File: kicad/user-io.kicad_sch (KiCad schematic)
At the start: 46 parts, among them J1 USB1, J2 Conn_01x30, J3 Conn_01x30, SW1 PTS815, U1 MIMXRT1171DVMAB, U2 MAYA-W166-00B, U3 LSM6DSV, U4 LIS2MDL, U5 RTMC-G2-4IQ48, Y1 8MHz

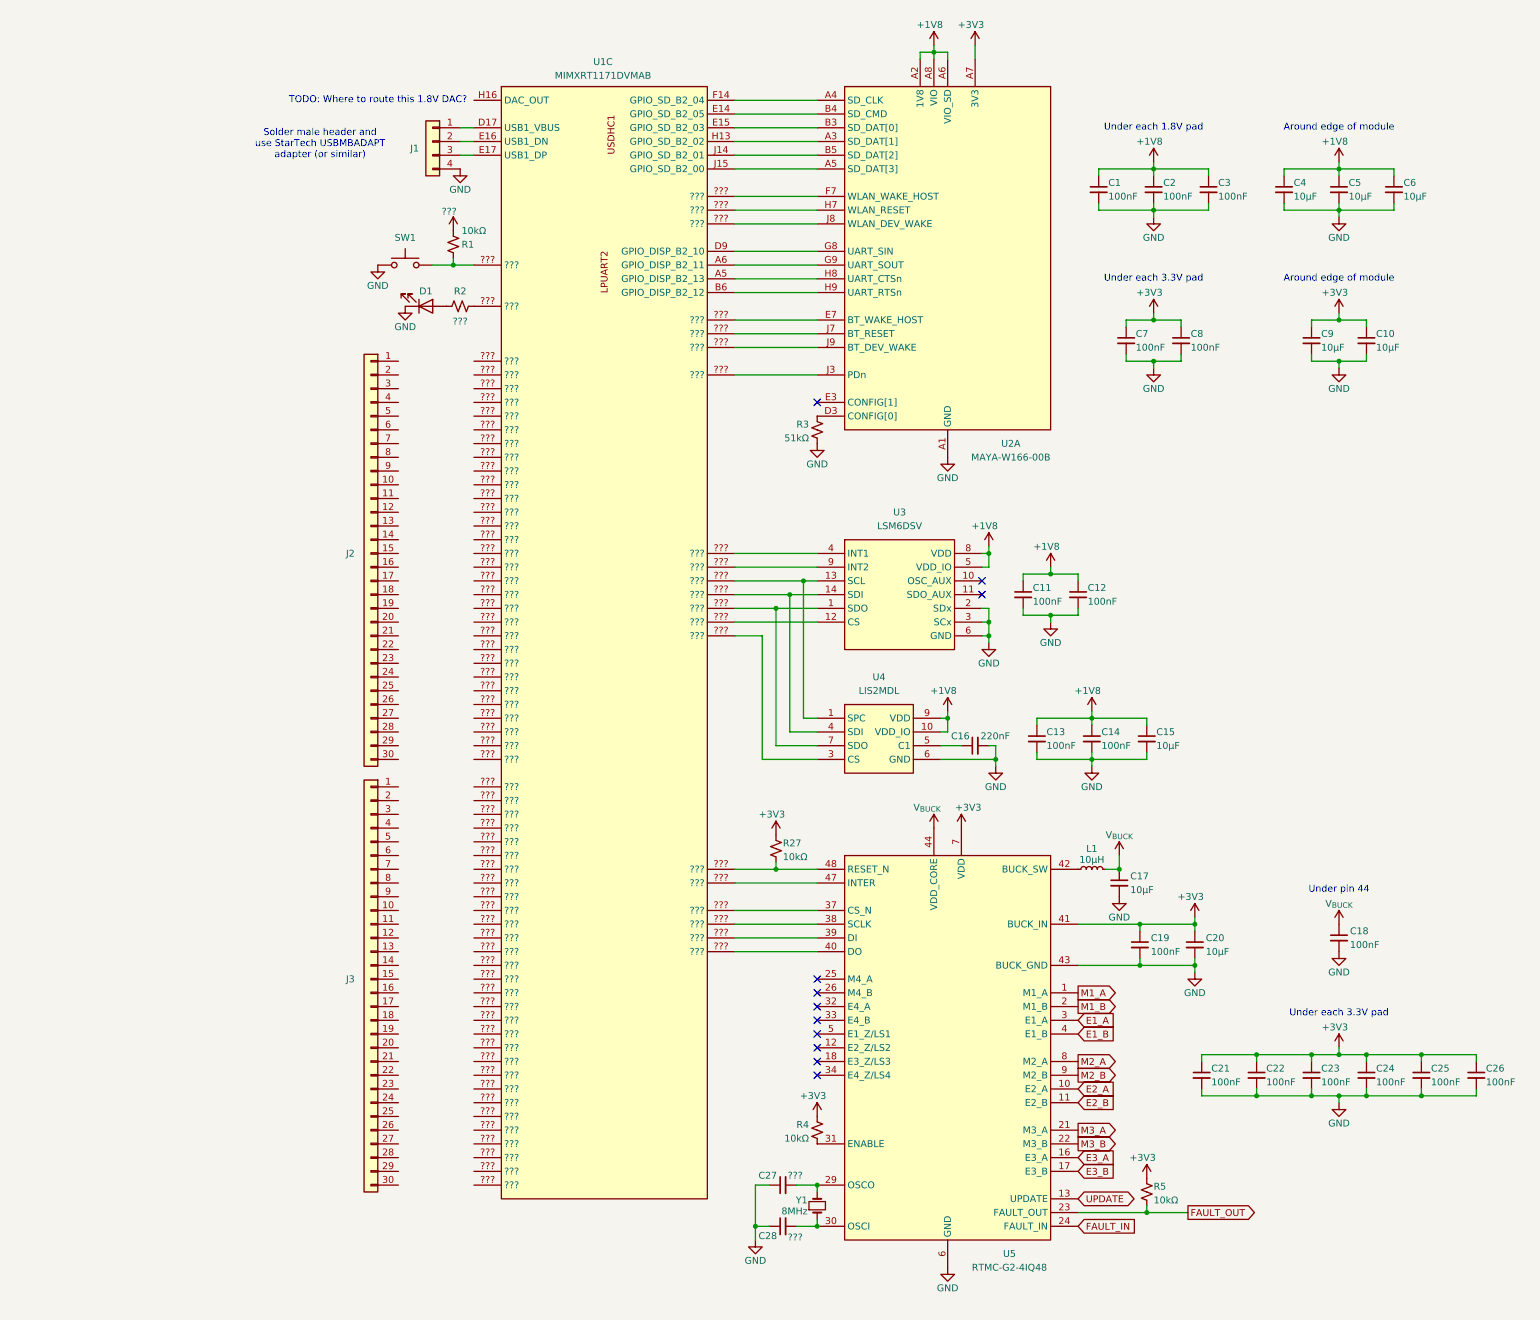
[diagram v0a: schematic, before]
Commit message: added several footprints
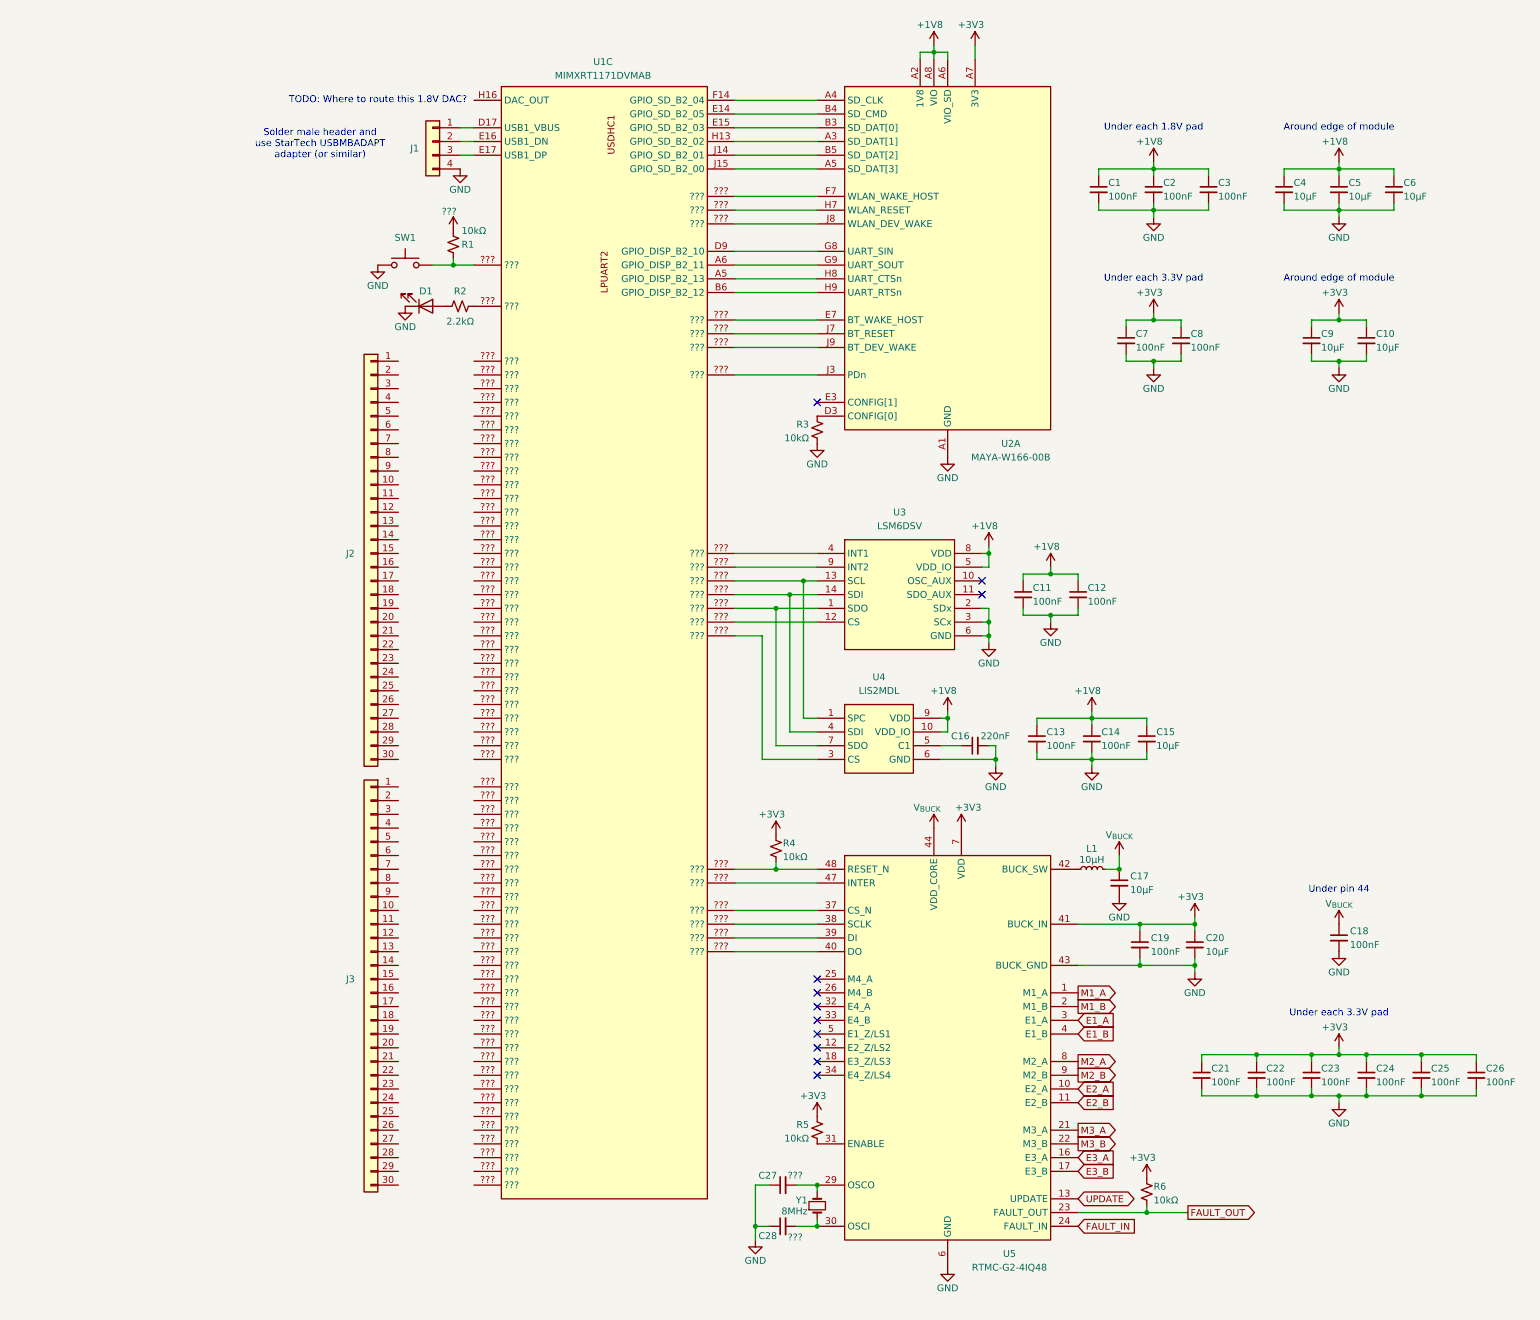
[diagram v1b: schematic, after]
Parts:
- C1, C11, C12, C13, C14, C18, C19, C2, C21, C22, C23, C24, C25, C26, C3, C7, C8: footprint (none) -> Capacitor_SMD:C_0201_0603Metric
- C10, C15, C17, C20, C4, C5, C6, C9: footprint (none) -> Capacitor_SMD:C_0402_1005Metric
- D1: footprint (none) -> LED_SMD:LED_0603_1608Metric
- J1: footprint (none) -> project_footprints:Header-1x04
- J2, J3: value Conn_01x30 -> (none); footprint (none) -> project_footprints:Header-1x30
- R1: footprint (none) -> Resistor_SMD:R_0201_0603Metric
- R2: value ??? -> 2.2kΩ; footprint (none) -> Resistor_SMD:R_0201_0603Metric
- R3: value 51kΩ -> 10kΩ; footprint (none) -> Resistor_SMD:R_0201_0603Metric
- R4: renamed from R27; footprint (none) -> Resistor_SMD:R_0201_0603Metric
- R5: renamed from R4; footprint (none) -> Resistor_SMD:R_0201_0603Metric
- R6: renamed from R5; footprint (none) -> Resistor_SMD:R_0201_0603Metric
- U1: footprint Package_BGA:MAPBGA-289_14x14mm_Layout17x17_P0.8mm -> project_footprints:MIMXRT1171DVMAB
- U3: footprint (none) -> project_footprints:LSM6DSV
- U4: footprint (none) -> project_footprints:LIS2MDL
- U5: footprint (none) -> project_footprints:RTMC-G2-4IQ48
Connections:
- net at U1.???: now also U2.J9 (BT_DEV_WAKE)

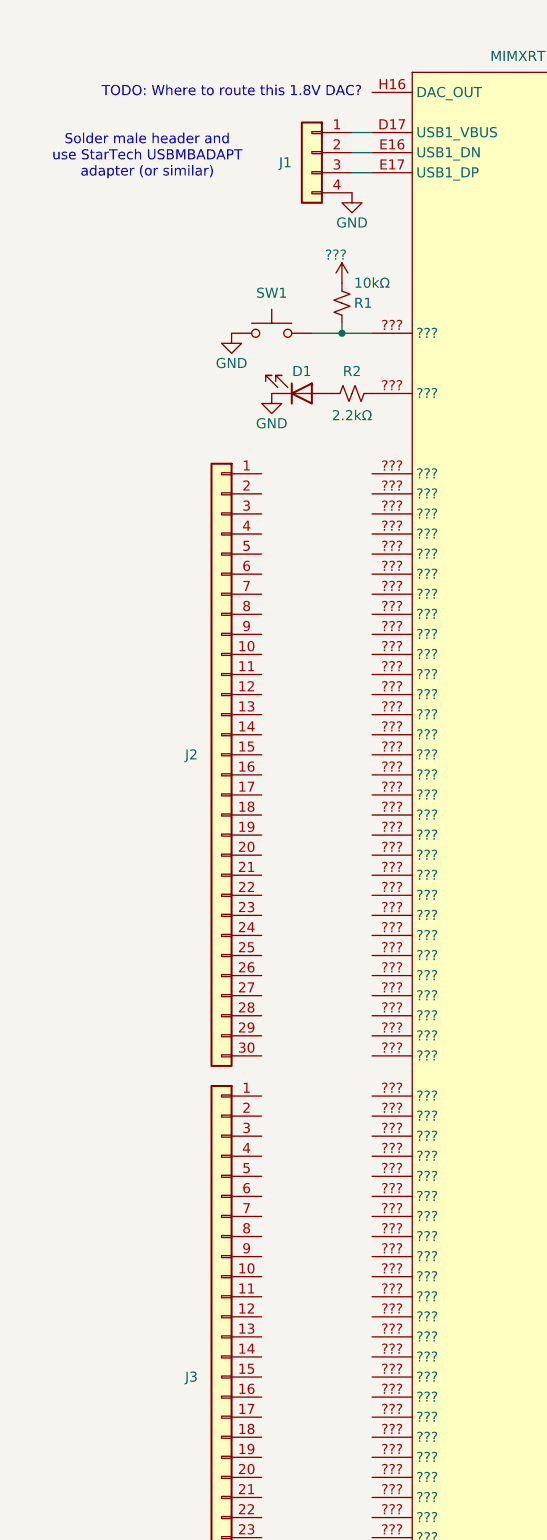
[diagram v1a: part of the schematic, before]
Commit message: added RTC battery connector
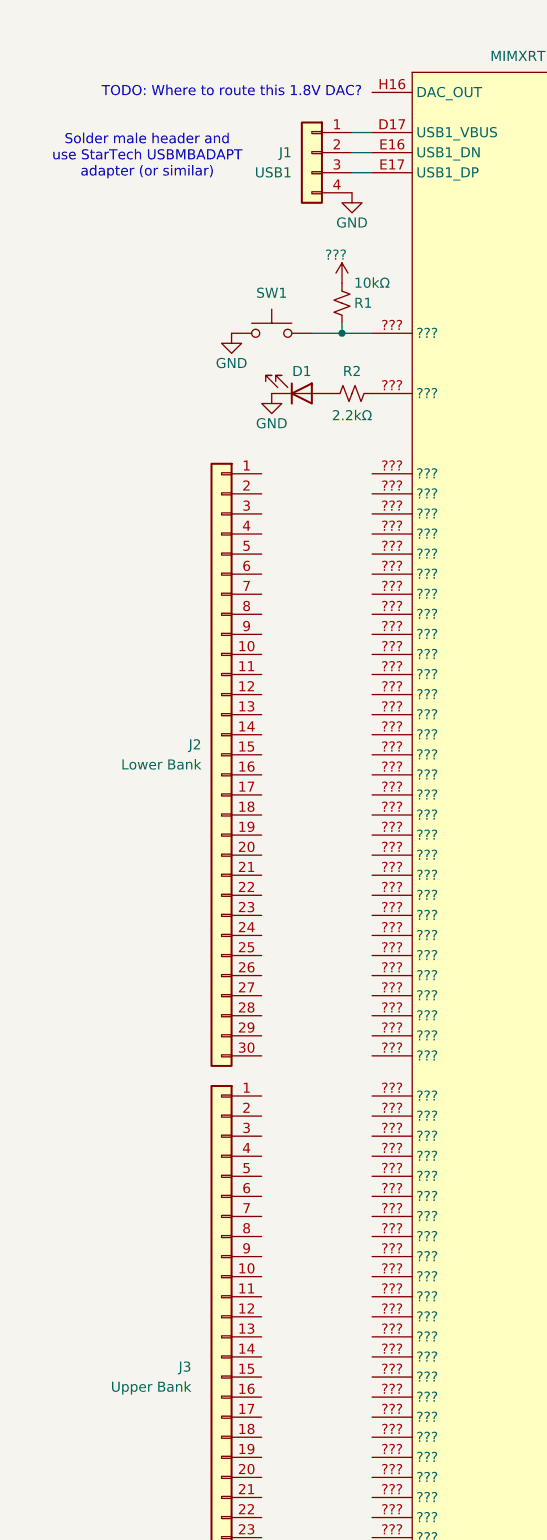
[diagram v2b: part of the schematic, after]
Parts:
- J2: value (none) -> Lower Bank
- J3: value (none) -> Upper Bank
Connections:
- net at U1.???: now also U2.J9 (BT_DEV_WAKE)
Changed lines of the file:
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@@
 		(dnp no)
 		(property "Reference" "J3"
-			(at 86.36 194.31 0)
+			(at 86.36 193.04 0)
 			(show_name no)
 			(do_not_autoplace no)
@@
 					(size 1.27 1.27)
 				)
+				(justify left)
 			)
 		)
-		(property "Value" ""
-			(at 90.17 237.998 0)
-			(hide yes)
+		(property "Value" "Upper Bank"
+			(at 86.36 195.58 0)
 			(show_name no)
 			(do_not_autoplace no)
@@
 					(size 1.27 1.27)
 				)
+				(justify left)
 			)
 		)
@@
 		(dnp no)
 		(property "Reference" "J1"
-			(at 99.06 40.64 0)
+			(at 99.06 39.37 0)
 			(show_name no)
 			(do_not_autoplace no)
@@
 		(property "Value" "USB1"
 			(at 99.06 41.9099 0)
-			(hide yes)
 			(show_name no)
 			(do_not_autoplace no)
@@
 		(dnp no)
 		(property "Reference" "J2"
-			(at 86.36 115.57 0)
+			(at 87.63 114.3 0)
 			(show_name no)
 			(do_not_autoplace no)
@@
 					(size 1.27 1.27)
 				)
+				(justify left)
 			)
 		)
-		(property "Value" ""
-			(at 90.17 159.258 0)
-			(hide yes)
+		(property "Value" "Lower Bank"
+			(at 87.63 116.84 0)
 			(show_name no)
 			(do_not_autoplace no)
@@
 					(size 1.27 1.27)
 				)
+				(justify left)
 			)
 		)

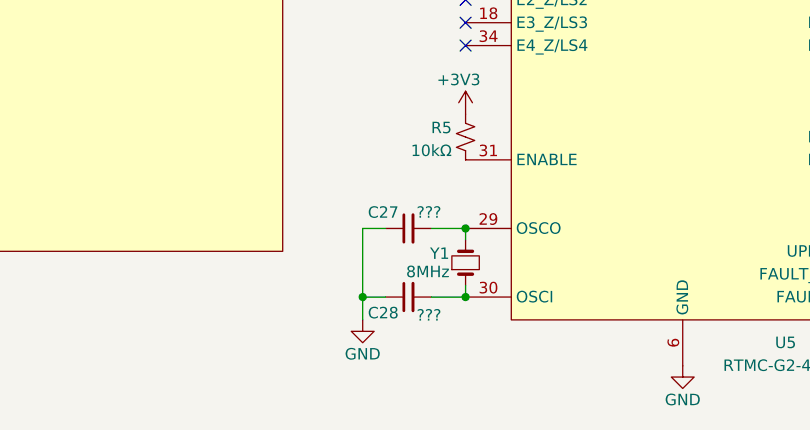
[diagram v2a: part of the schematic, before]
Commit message: added crystal footprints
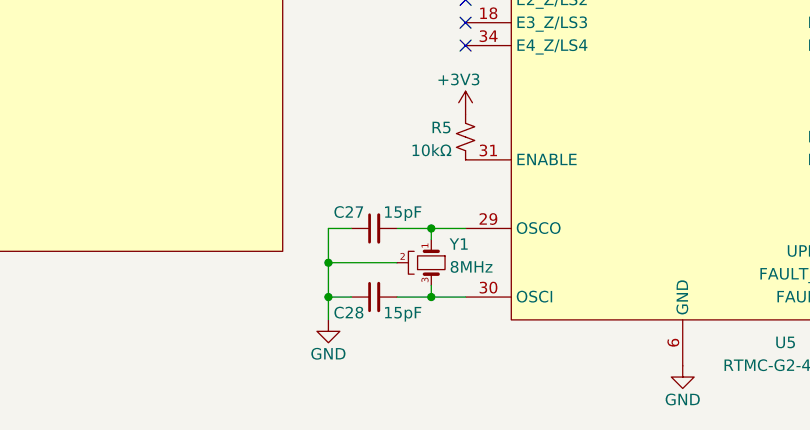
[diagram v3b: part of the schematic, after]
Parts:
- removed Y1: 8MHz, symbol Device:Crystal_Small
- added Y1: 8MHz, project_footprints:Crystal-4-Pin, symbol project_symbols:Crystal_GND24_Small
- C27, C28: value ??? -> 15pF; footprint (none) -> Capacitor_SMD:C_0402_1005Metric
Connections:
- net GND: now also Y1.2 (GND), Y1.4 (GND)
- net at C27.2, U5.29 (OSCO): now also Y1.1
- net at C28.2, U5.30 (OSCI): now also Y1.3
- net at U1.???: now also U2.J9 (BT_DEV_WAKE)

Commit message: added inductor footprints
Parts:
- L1: footprint (none) -> Inductor_SMD:L_1008_2520Metric
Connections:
- net at U1.???: now also U2.J9 (BT_DEV_WAKE)
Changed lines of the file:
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@@
 			)
 		)
-		(property "Footprint" ""
+		(property "Footprint" "Inductor_SMD:L_1008_2520Metric"
 			(at 223.52 173.99 0)
 			(hide yes)
